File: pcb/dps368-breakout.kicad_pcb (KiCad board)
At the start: 2 copper layers, 13.7 x 13.7 mm, 8 parts, among them J1 Conn_01x05_Pin, U1 DPS368XTSA1

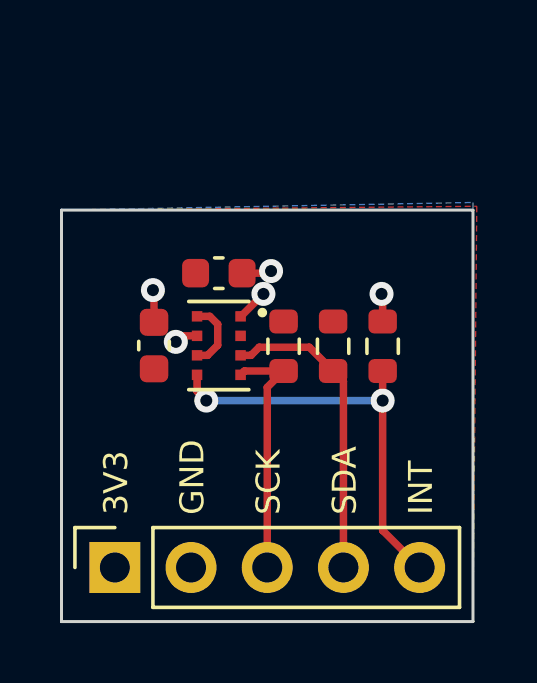
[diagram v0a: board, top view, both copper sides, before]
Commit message: Added mounting hole
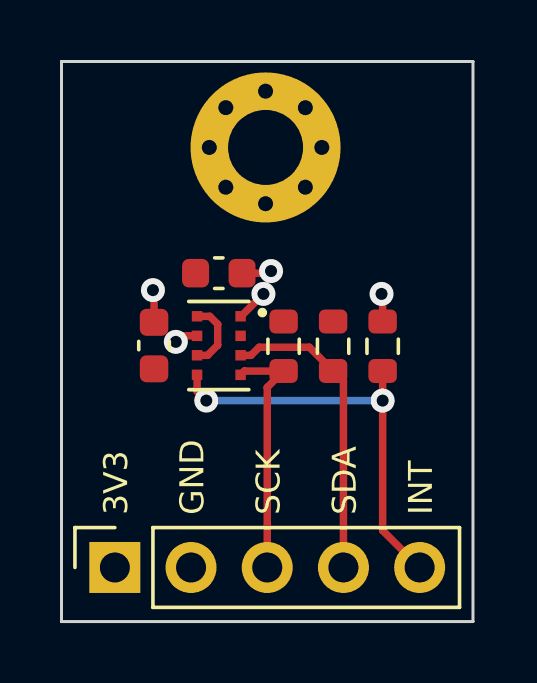
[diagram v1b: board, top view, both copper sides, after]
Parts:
- added H1: MountingHole, MountingHole:MountingHole_2.5mm_Pad_Via, F.Cu at (132.4, 93.4)
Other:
- board size 13.7 x 13.7 mm -> 13.7 x 18.7 mm
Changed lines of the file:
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@@
     )
   )
+  (footprint "MountingHole:MountingHole_2.5mm_Pad_Via" (layer "F.Cu")
+    (at 132.405175 93.416175)
+    (descr "Mounting Hole 2.5mm")
+    (tags "mounting hole 2.5mm")
+    (property "Sheetfile" "dps368-breakout.kicad_sch")
+    (property "Sheetname" "")
+    (property "ki_description" "Mounting Hole without connection")
+    (property "ki_keywords" "mounting hole")
+    (attr exclude_from_pos_files)
+    (fp_text reference "H1" (at 0 -3.5) (layer "F.SilkS") hide
+        (effects (font (size 1 1) (thickness 0.15)))
+    )
+    (fp_text value "MountingHole" (at 0 3.5) (layer "F.Fab")
+        (effects (font (size 1 1) (thickness 0.15)))
+    )
+    (fp_text user "${REFERENCE}" (at 0 0) (layer "F.Fab")
+        (effects (font (size 1 1) (thickness 0.15)))
+    )
+    (fp_circle (center 0 0) (end 2.5 0)
+      (stroke (width 0.15) (type solid)) (fill none) (layer "Cmts.User"))
+    (fp_circle (center 0 0) (end 2.75 0)
+      (stroke (width 0.05) (type solid)) (fill none) (layer "F.CrtYd"))
+    (pad "1" thru_hole circle (at -1.875 0) (size 0.8 0.8) (drill 0.5) (layers "*.Cu" "*.Mask"))
+    (pad "1" thru_hole circle (at -1.325825 -1.325825) (size 0.8 0.8) (drill 0.5) (layers "*.Cu" "*.Mask"))
+    (pad "1" thru_hole circle (at -1.325825 1.325825) (size 0.8 0.8) (drill 0.5) (layers "*.Cu" "*.Mask"))
+    (pad "1" thru_hole circle (at 0 -1.875) (size 0.8 0.8) (drill 0.5) (layers "*.Cu" "*.Mask"))
+    (pad "1" thru_hole circle (at 0 0) (size 5 5) (drill 2.5) (layers "*.Cu" "*.Mask"))
+    (pad "1" thru_hole circle (at 0 1.875) (size 0.8 0.8) (drill 0.5) (layers "*.Cu" "*.Mask"))
+    (pad "1" thru_hole circle (at 1.325825 -1.325825) (size 0.8 0.8) (drill 0.5) (layers "*.Cu" "*.Mask"))
+    (pad "1" thru_hole circle (at 1.325825 1.325825) (size 0.8 0.8) (drill 0.5) (layers "*.Cu" "*.Mask"))
+    (pad "1" thru_hole circle (at 1.875 0) (size 0.8 0.8) (drill 0.5) (layers "*.Cu" "*.Mask"))
+  )
   (footprint "Capacitor_SMD:C_0603_1608Metric" (layer "F.Cu")
     (at 128.688 100.02 90)
@@
       (stroke (width 0) (type solid)) (fill solid) (layer "B.SilkS"))
   )
-  (gr_line (start 125.603 95.504) (end 139.319 95.504)
+  (gr_line (start 125.603 90.551) (end 139.319 90.551)
     (stroke (width 0.1) (type default)) (layer "Edge.Cuts"))
   (gr_line (start 139.319 109.22) (end 125.603 109.22)
     (stroke (width 0.1) (type default)) (layer "Edge.Cuts"))
-  (gr_line (start 139.319 95.504) (end 139.319 109.22)
+  (gr_line (start 139.319 90.551) (end 139.319 109.22)
     (stroke (width 0.1) (type default)) (layer "Edge.Cuts"))
-  (gr_line (start 125.603 109.22) (end 125.603 95.504)
+  (gr_line (start 125.603 109.22) (end 125.603 90.551)
     (stroke (width 0.1) (type default)) (layer "Edge.Cuts"))
   (gr_text "DPS368 Breakout" (at 138.684 99.441) (layer "B.SilkS")
@@
     (polygon
       (pts
-        (xy 125.603 95.504)
-        (xy 139.446 95.377)
+        (xy 125.603 90.551)
+        (xy 139.319 90.551)
         (xy 139.319 109.22)
         (xy 125.603 109.22)
@@
     (polygon
       (pts
-        (xy 125.603 95.504)
-        (xy 139.319 95.25)
+        (xy 125.603 90.551)
+        (xy 139.319 90.551)
         (xy 139.319 109.22)
         (xy 125.603 109.22)
